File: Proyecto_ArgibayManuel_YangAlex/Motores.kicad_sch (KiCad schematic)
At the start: 12 parts, among them K1 RT314012, K2 RT314012, Q1 2N2222, Q2 2N2222, U6 DRV8871DDA, U7 DRV8871DDA

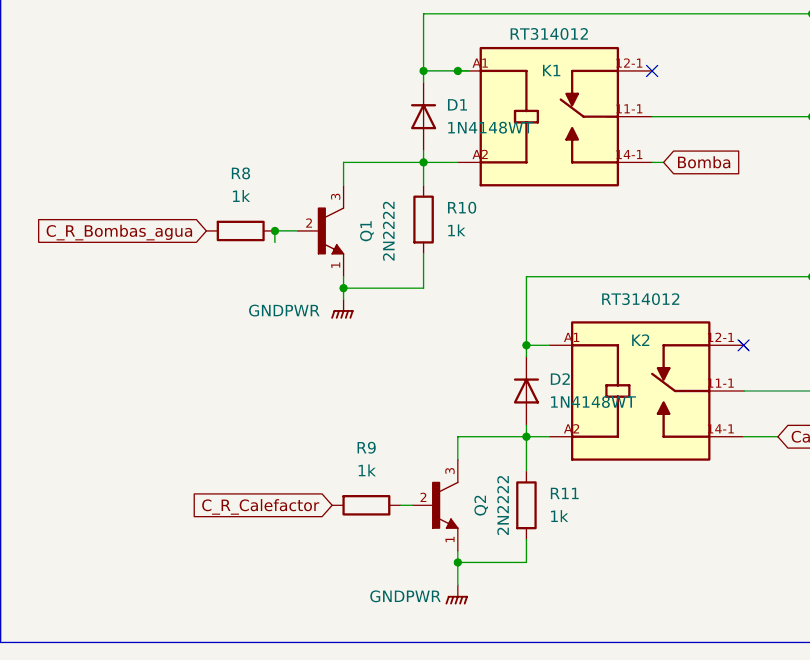
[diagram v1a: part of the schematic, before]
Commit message: Cambio del sensor
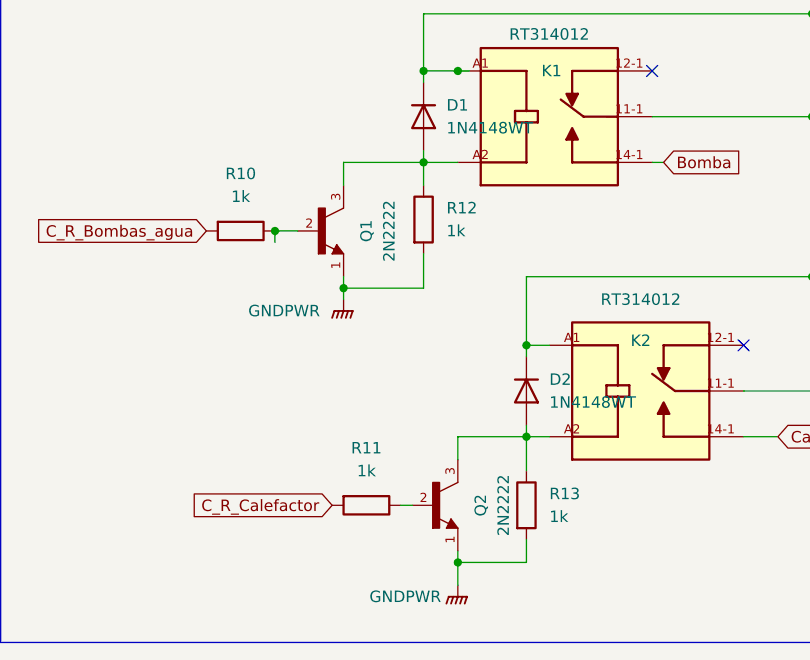
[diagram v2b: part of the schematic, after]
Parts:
- renumbered R8 to R10, R9 to R11, R10 to R12, R11 to R13
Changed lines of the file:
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@@
 		(on_board yes)
 		(dnp no)
-		(property "Reference" "#PWR030"
+		(property "Reference" "#PWR035"
 			(at 186.69 132.08 0)
 			(effects
@@
 			(project "Proyecto_ArgibayManuel_YangAlex"
 				(path "/b2dde924-33f5-41ab-a1bf-811873450a89/4b87e8bb-9014-4438-949a-51563e216ea6"
-					(reference "#PWR030")
+					(reference "#PWR035")
 					(unit 1)
 				)
@@
 		(dnp no)
 		(fields_autoplaced yes)
-		(property "Reference" "R8"
+		(property "Reference" "R10"
 			(at 71.12 87.63 90)
 			(effects
@@
 			(project "Proyecto_ArgibayManuel_YangAlex"
 				(path "/b2dde924-33f5-41ab-a1bf-811873450a89/4b87e8bb-9014-4438-949a-51563e216ea6"
-					(reference "R8")
+					(reference "R10")
 					(unit 1)
 				)
@@
 		(on_board yes)
 		(dnp no)
-		(property "Reference" "#PWR028"
+		(property "Reference" "#PWR033"
 			(at 95.25 138.43 0)
 			(effects
@@
 			(project "Proyecto_ArgibayManuel_YangAlex"
 				(path "/b2dde924-33f5-41ab-a1bf-811873450a89/4b87e8bb-9014-4438-949a-51563e216ea6"
-					(reference "#PWR028")
+					(reference "#PWR033")
 					(unit 1)
 				)
@@
 		(on_board yes)
 		(dnp no)
-		(property "Reference" "#PWR029"
+		(property "Reference" "#PWR034"
 			(at 185.42 101.6 0)
 			(effects
@@
 			(project "Proyecto_ArgibayManuel_YangAlex"
 				(path "/b2dde924-33f5-41ab-a1bf-811873450a89/4b87e8bb-9014-4438-949a-51563e216ea6"
-					(reference "#PWR029")
+					(reference "#PWR034")
 					(unit 1)
 				)
@@
 		(dnp no)
 		(fields_autoplaced yes)
-		(property "Reference" "R11"
+		(property "Reference" "R13"
 			(at 105.41 123.1899 0)
 			(effects
@@
 			(project "Proyecto_ArgibayManuel_YangAlex"
 				(path "/b2dde924-33f5-41ab-a1bf-811873450a89/4b87e8bb-9014-4438-949a-51563e216ea6"
-					(reference "R11")
+					(reference "R13")
 					(unit 1)
 				)
@@
 		(on_board yes)
 		(dnp no)
-		(property "Reference" "#PWR027"
+		(property "Reference" "#PWR032"
 			(at 82.55 106.68 0)
 			(effects
@@
 			(project "Proyecto_ArgibayManuel_YangAlex"
 				(path "/b2dde924-33f5-41ab-a1bf-811873450a89/4b87e8bb-9014-4438-949a-51563e216ea6"
-					(reference "#PWR027")
+					(reference "#PWR032")
 					(unit 1)
 				)
@@
 		(dnp no)
 		(fields_autoplaced yes)
-		(property "Reference" "R9"
+		(property "Reference" "R11"
 			(at 85.09 118.11 90)
 			(effects
@@
 			(project "Proyecto_ArgibayManuel_YangAlex"
 				(path "/b2dde924-33f5-41ab-a1bf-811873450a89/4b87e8bb-9014-4438-949a-51563e216ea6"
-					(reference "R9")
+					(reference "R11")
 					(unit 1)
 				)
@@
 		(dnp no)
 		(fields_autoplaced yes)
-		(property "Reference" "R10"
+		(property "Reference" "R12"
 			(at 93.98 91.4399 0)
 			(effects
@@
 			(project "Proyecto_ArgibayManuel_YangAlex"
 				(path "/b2dde924-33f5-41ab-a1bf-811873450a89/4b87e8bb-9014-4438-949a-51563e216ea6"
-					(reference "R10")
+					(reference "R12")
 					(unit 1)
 				)
